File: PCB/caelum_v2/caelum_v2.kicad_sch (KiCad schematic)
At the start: 40 parts, among them J1 SS445P, J2 i2C Bus2, J4 Batt, J5 DRV5032DULPG(M), J7 I2C BUS1, J8 DS18B20, Q1 FS8205A-FC, Q2 BSS138, Q3 Si2323DS, U1 DW01A, U2 MCP1825S, U3 ESP32-H2-SUPERMINI, U5 LPS22HB

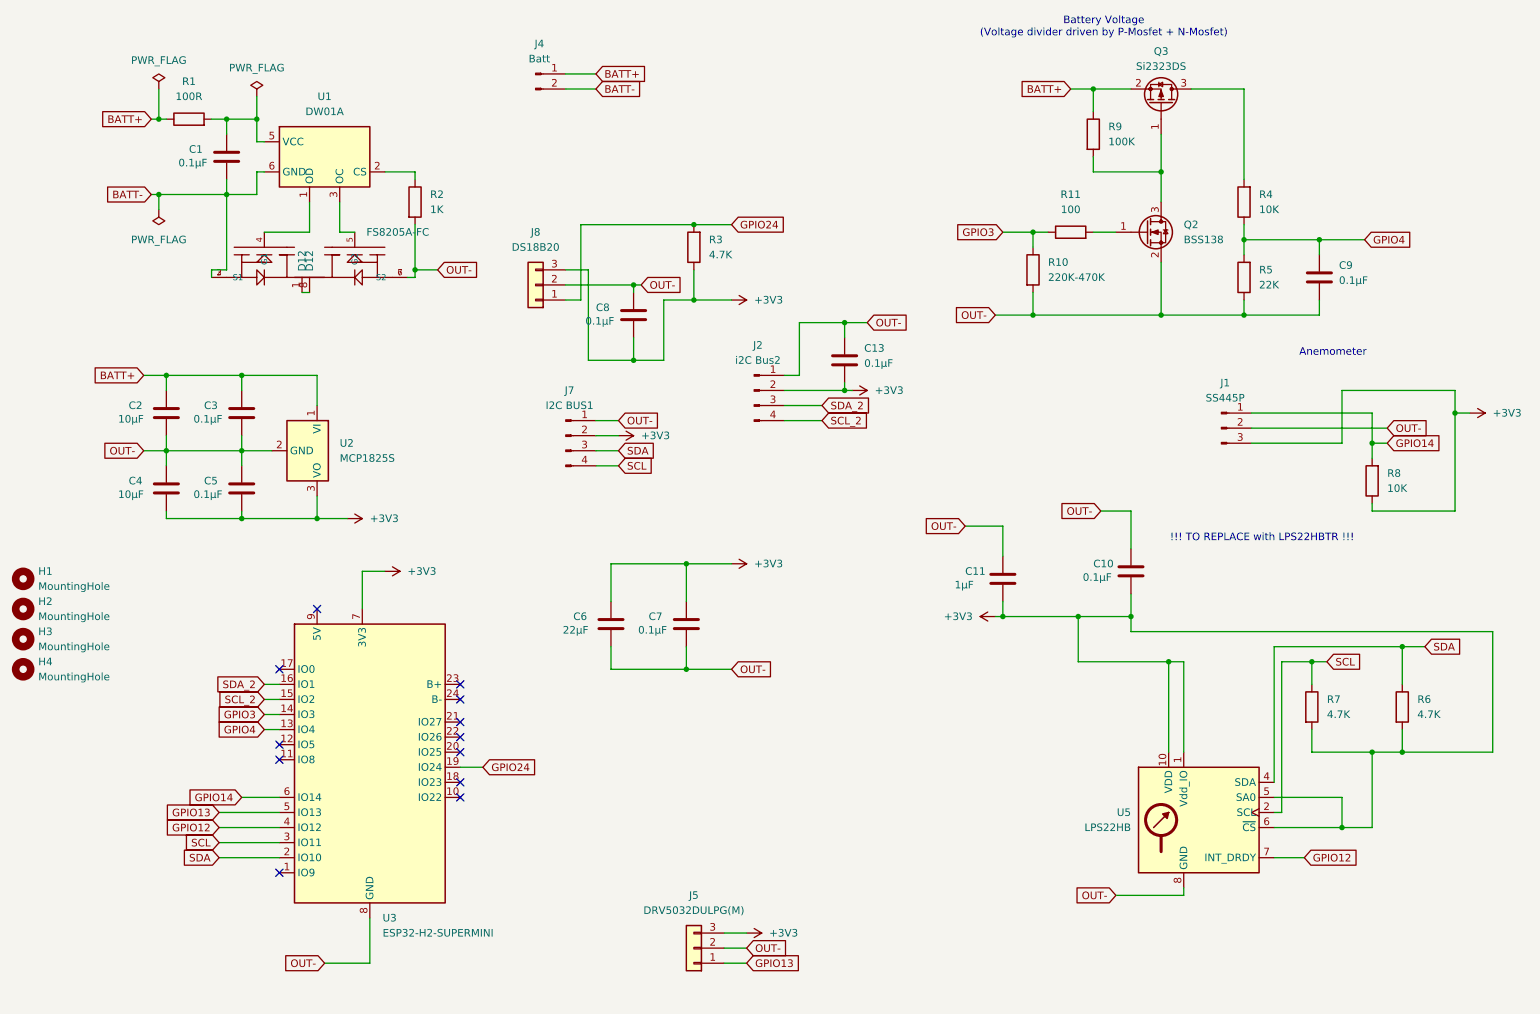
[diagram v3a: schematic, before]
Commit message: Update battery voltage divider values and improve LPS22HB driver comments for clarity
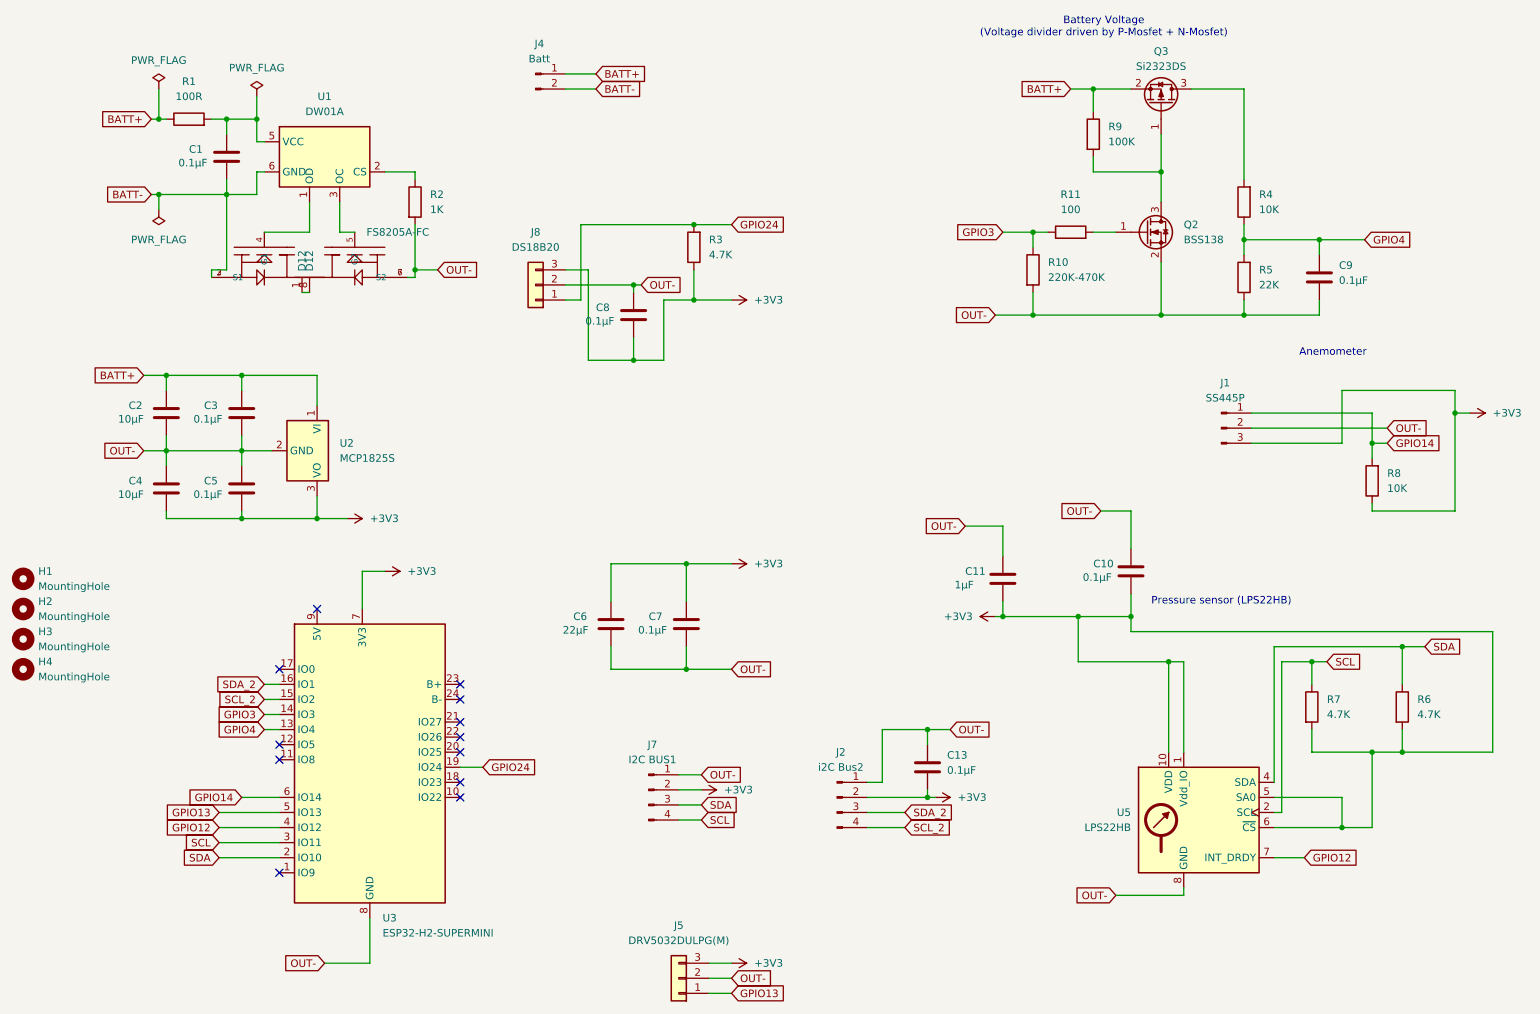
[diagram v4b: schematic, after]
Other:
- note added: "Pressure sensor (LPS22HB)"
- note removed: "!!! TO REPLACE with LPS22HBTR !!!"
- moved on the sheet: C13, J2, J5, J7
